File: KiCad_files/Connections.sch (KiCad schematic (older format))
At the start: 4 parts, among them U1 XC7A35T_CSG325

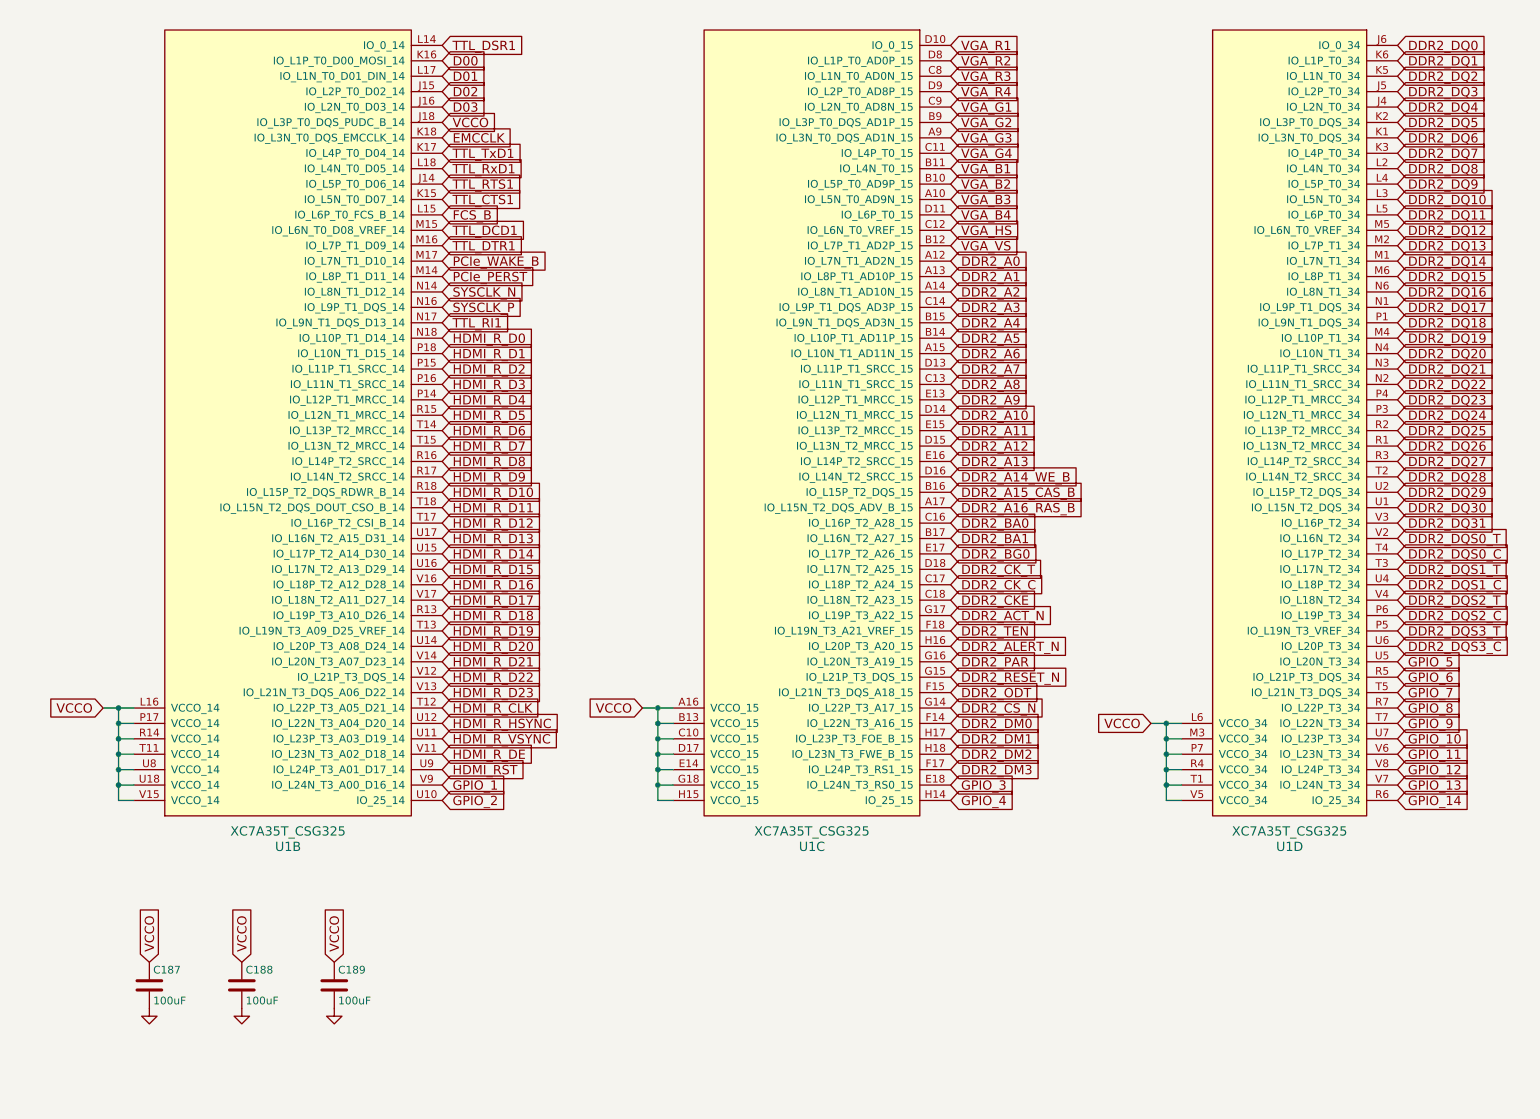
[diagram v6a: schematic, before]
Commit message: HDMI_VGA is good. Need 5V for HDMI
TODO: DDR2, connections, power
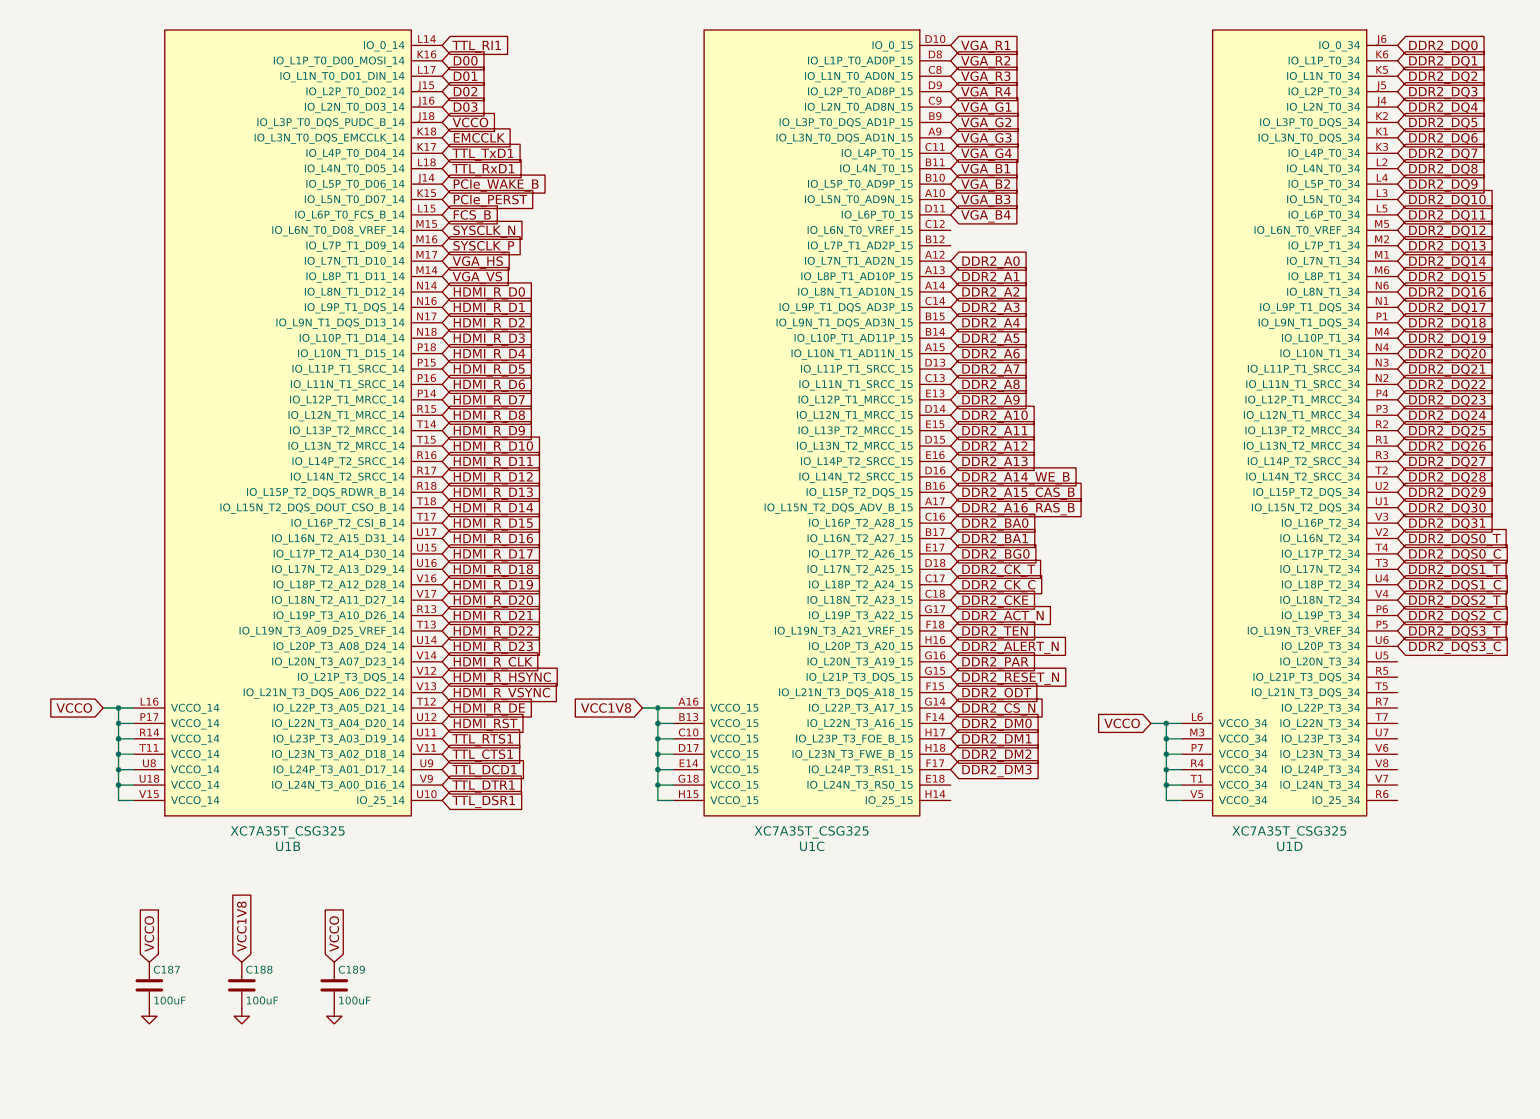
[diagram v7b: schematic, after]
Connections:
- net GPIO_1 is gone; now on net TTL_DTR1: U1.V9 (IO_L24N_T3_A00_D16_14)
- net GPIO_2 is gone; now on net TTL_DSR1: U1.U10 (IO_25_14)
- net HDMI_RST: now also U1.U12 (IO_L22N_T3_A04_D20_14); no longer U1.U9 (IO_L24P_T3_A01_D17_14)
- net HDMI_R_CLK: now also U1.V14 (IO_L20N_T3_A07_D23_14); no longer U1.T12 (IO_L22P_T3_A05_D21_14)
- net HDMI_R_D0: now also U1.N14 (IO_L8N_T1_D12_14); no longer U1.N18 (IO_L10P_T1_D14_14)
- net HDMI_R_D1: now also U1.N16 (IO_L9P_T1_DQS_14); no longer U1.P18 (IO_L10N_T1_D15_14)
- net HDMI_R_D10: now also U1.T15 (IO_L13N_T2_MRCC_14); no longer U1.R18 (IO_L15P_T2_DQS_RDWR_B_14)
- net HDMI_R_D11: now also U1.R16 (IO_L14P_T2_SRCC_14); no longer U1.T18 (IO_L15N_T2_DQS_DOUT_CSO_B_14)
- net HDMI_R_D12: now also U1.R17 (IO_L14N_T2_SRCC_14); no longer U1.T17 (IO_L16P_T2_CSI_B_14)
- net HDMI_R_D13: now also U1.R18 (IO_L15P_T2_DQS_RDWR_B_14); no longer U1.U17 (IO_L16N_T2_A15_D31_14)
- net HDMI_R_D14: now also U1.T18 (IO_L15N_T2_DQS_DOUT_CSO_B_14); no longer U1.U15 (IO_L17P_T2_A14_D30_14)
- net HDMI_R_D15: now also U1.T17 (IO_L16P_T2_CSI_B_14); no longer U1.U16 (IO_L17N_T2_A13_D29_14)
- net HDMI_R_D16: now also U1.U17 (IO_L16N_T2_A15_D31_14); no longer U1.V16 (IO_L18P_T2_A12_D28_14)
- net HDMI_R_D17: now also U1.U15 (IO_L17P_T2_A14_D30_14); no longer U1.V17 (IO_L18N_T2_A11_D27_14)
- net HDMI_R_D18: now also U1.U16 (IO_L17N_T2_A13_D29_14); no longer U1.R13 (IO_L19P_T3_A10_D26_14)
- net HDMI_R_D19: now also U1.V16 (IO_L18P_T2_A12_D28_14); no longer U1.T13 (IO_L19N_T3_A09_D25_VREF_14)
- net HDMI_R_D2: now also U1.N17 (IO_L9N_T1_DQS_D13_14); no longer U1.P15 (IO_L11P_T1_SRCC_14)
- net HDMI_R_D20: now also U1.V17 (IO_L18N_T2_A11_D27_14); no longer U1.U14 (IO_L20P_T3_A08_D24_14)
- net HDMI_R_D21: now also U1.R13 (IO_L19P_T3_A10_D26_14); no longer U1.V14 (IO_L20N_T3_A07_D23_14)
- net HDMI_R_D22: now also U1.T13 (IO_L19N_T3_A09_D25_VREF_14); no longer U1.V12 (IO_L21P_T3_DQS_14)
- net HDMI_R_D23: now also U1.U14 (IO_L20P_T3_A08_D24_14); no longer U1.V13 (IO_L21N_T3_DQS_A06_D22_14)
- net HDMI_R_D3: now also U1.N18 (IO_L10P_T1_D14_14); no longer U1.P16 (IO_L11N_T1_SRCC_14)
- net HDMI_R_D4: now also U1.P18 (IO_L10N_T1_D15_14); no longer U1.P14 (IO_L12P_T1_MRCC_14)
- net HDMI_R_D5: now also U1.P15 (IO_L11P_T1_SRCC_14); no longer U1.R15 (IO_L12N_T1_MRCC_14)
- net HDMI_R_D6: now also U1.P16 (IO_L11N_T1_SRCC_14); no longer U1.T14 (IO_L13P_T2_MRCC_14)
- net HDMI_R_D7: now also U1.P14 (IO_L12P_T1_MRCC_14); no longer U1.T15 (IO_L13N_T2_MRCC_14)
- net HDMI_R_D8: now also U1.R15 (IO_L12N_T1_MRCC_14); no longer U1.R16 (IO_L14P_T2_SRCC_14)
- net HDMI_R_D9: now also U1.T14 (IO_L13P_T2_MRCC_14); no longer U1.R17 (IO_L14N_T2_SRCC_14)
- net HDMI_R_DE: now also U1.T12 (IO_L22P_T3_A05_D21_14); no longer U1.V11 (IO_L23N_T3_A02_D18_14)
- net HDMI_R_HSYNC: now also U1.V12 (IO_L21P_T3_DQS_14); no longer U1.U12 (IO_L22N_T3_A04_D20_14)
- net HDMI_R_VSYNC: now also U1.V13 (IO_L21N_T3_DQS_A06_D22_14); no longer U1.U11 (IO_L23P_T3_A03_D19_14)
- net PCIe_PERST: now also U1.K15 (IO_L5N_T0_D07_14); no longer U1.M14 (IO_L8P_T1_D11_14)
- net PCIe_WAKE_B: now also U1.J14 (IO_L5P_T0_D06_14); no longer U1.M17 (IO_L7N_T1_D10_14)
- net SYSCLK_N: now also U1.M15 (IO_L6N_T0_D08_VREF_14); no longer U1.N14 (IO_L8N_T1_D12_14)
- net SYSCLK_P: now also U1.M16 (IO_L7P_T1_D09_14); no longer U1.N16 (IO_L9P_T1_DQS_14)
- net TTL_CTS1: now also U1.V11 (IO_L23N_T3_A02_D18_14); no longer U1.K15 (IO_L5N_T0_D07_14)
- net TTL_DCD1: now also U1.U9 (IO_L24P_T3_A01_D17_14); no longer U1.M15 (IO_L6N_T0_D08_VREF_14)
- net TTL_DSR1: no longer U1.L14 (IO_0_14)
- net TTL_DTR1: no longer U1.M16 (IO_L7P_T1_D09_14)
- net TTL_RI1: now also U1.L14 (IO_0_14); no longer U1.N17 (IO_L9N_T1_DQS_D13_14)
- net TTL_RTS1: now also U1.U11 (IO_L23P_T3_A03_D19_14); no longer U1.J14 (IO_L5P_T0_D06_14)
- net VCCO: no longer C188.1, U1.A16 (VCCO_15), U1.B13 (VCCO_15), U1.C10 (VCCO_15), U1.D17 (VCCO_15), U1.E14 (VCCO_15), U1.G18 (VCCO_15), U1.H15 (VCCO_15)
- net VGA_HS: now also U1.M17 (IO_L7N_T1_D10_14); no longer U1.C12 (IO_L6N_T0_VREF_15)
- net VGA_VS: now also U1.M14 (IO_L8P_T1_D11_14); no longer U1.B12 (IO_L7P_T1_AD2P_15)
- net GPIO_10: no longer names the net of U1.U7 (IO_L23P_T3_34)
- net GPIO_11: no longer names the net of U1.V6 (IO_L23N_T3_34)
- net GPIO_12: no longer names the net of U1.V8 (IO_L24P_T3_34)
- net GPIO_13: no longer names the net of U1.V7 (IO_L24N_T3_34)
- net GPIO_14: no longer names the net of U1.R6 (IO_25_34)
- net GPIO_3: no longer names the net of U1.E18 (IO_L24N_T3_RS0_15)
- net GPIO_4: no longer names the net of U1.H14 (IO_25_15)
- net GPIO_5: no longer names the net of U1.U5 (IO_L20N_T3_34)
- net GPIO_6: no longer names the net of U1.R5 (IO_L21P_T3_DQS_34)
- net GPIO_7: no longer names the net of U1.T5 (IO_L21N_T3_DQS_34)
- net GPIO_8: no longer names the net of U1.R7 (IO_L22P_T3_34)
- net GPIO_9: no longer names the net of U1.T7 (IO_L22N_T3_34)
- new net VCC1V8: C188.1, U1.A16 (VCCO_15), U1.B13 (VCCO_15), U1.C10 (VCCO_15), U1.D17 (VCCO_15), U1.E14 (VCCO_15), U1.G18 (VCCO_15), U1.H15 (VCCO_15)
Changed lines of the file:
@@
 $Descr A4 11693 8268
 encoding utf-8
-Sheet 6 10
+Sheet 6 9
 Title "Reconfigurable Application-Specific Accelerator Card"
 Date "2018-11-27"
@@
 	1    0    0    -1
 $EndComp
-Text GLabel 3200 2500 2    60   Input ~ 0
+Text GLabel 3200 2000 2    60   Input ~ 0
 PCIe_WAKE_B
-Text GLabel 3200 2600 2    60   Input ~ 0
+Text GLabel 3200 2100 2    60   Input ~ 0
 PCIe_PERST
 Text GLabel 3200 1600 2    60   Input ~ 0
 VCCO
 Text GLabel 4500 5400 0    60   Input ~ 0
-VCCO
+VCC1V8
 Wire Wire Line
 	4500 5400 4600 5400
@@
 $EndComp
 Text GLabel 1900 7050 1    60   Input ~ 0
-VCCO
+VCC1V8
 $Comp
 L power:GND #PWR098
@@
 	7900 5600 8000 5600
 Connection ~ 7900 5600
+Text GLabel 3200 2700 2    60   Input ~ 0
+HDMI_R_D0
+Text GLabel 3200 2800 2    60   Input ~ 0
+HDMI_R_D1
+Text GLabel 3200 2900 2    60   Input ~ 0
+HDMI_R_D2
 Text GLabel 3200 3000 2    60   Input ~ 0
-HDMI_R_D0
+HDMI_R_D3
 Text GLabel 3200 3100 2    60   Input ~ 0
-HDMI_R_D1
+HDMI_R_D4
 Text GLabel 3200 3200 2    60   Input ~ 0
-HDMI_R_D2
+HDMI_R_D5
 Text GLabel 3200 3300 2    60   Input ~ 0
-HDMI_R_D3
+HDMI_R_D6
 Text GLabel 3200 3400 2    60   Input ~ 0
-HDMI_R_D4
+HDMI_R_D7
 Text GLabel 3200 3500 2    60   Input ~ 0
-HDMI_R_D5
+HDMI_R_D8
 Text GLabel 3200 3600 2    60   Input ~ 0
-HDMI_R_D6
+HDMI_R_D9
 Text GLabel 3200 3700 2    60   Input ~ 0
-HDMI_R_D7
+HDMI_R_D10
 Text GLabel 3200 3800 2    60   Input ~ 0
-HDMI_R_D8
+HDMI_R_D11
 Text GLabel 3200 3900 2    60   Input ~ 0
-HDMI_R_D9
+HDMI_R_D12
 Text GLabel 3200 4000 2    60   Input ~ 0
-HDMI_R_D10
+HDMI_R_D13
 Text GLabel 3200 4100 2    60   Input ~ 0
-HDMI_R_D11
+HDMI_R_D14
 Text GLabel 3200 4200 2    60   Input ~ 0
-HDMI_R_D12
+HDMI_R_D15
 Text GLabel 3200 4300 2    60   Input ~ 0
-HDMI_R_D13
+HDMI_R_D16
 Text GLabel 3200 4400 2    60   Input ~ 0
-HDMI_R_D14
+HDMI_R_D17
 Text GLabel 3200 4500 2    60   Input ~ 0
-HDMI_R_D15
+HDMI_R_D18
 Text GLabel 3200 4600 2    60   Input ~ 0
-HDMI_R_D16
+HDMI_R_D19
 Text GLabel 3200 4700 2    60   Input ~ 0
-HDMI_R_D17
+HDMI_R_D20
 Text GLabel 3200 4800 2    60   Input ~ 0
-HDMI_R_D18
+HDMI_R_D21
 Text GLabel 3200 4900 2    60   Input ~ 0
-HDMI_R_D19
+HDMI_R_D22
 Text GLabel 3200 5000 2    60   Input ~ 0
-HDMI_R_D20
+HDMI_R_D23
 Text GLabel 3200 5100 2    60   Input ~ 0
-HDMI_R_D21
+HDMI_R_CLK
+Text GLabel 3200 5500 2    60   Input ~ 0
+HDMI_RST
 Text GLabel 3200 5200 2    60   Input ~ 0
-HDMI_R_D22
+HDMI_R_HSYNC
 Text GLabel 3200 5300 2    60   Input ~ 0
-HDMI_R_D23
+HDMI_R_VSYNC
 Text GLabel 3200 5400 2    60   Input ~ 0
-HDMI_R_CLK
-Text GLabel 3200 5800 2    60   Input ~ 0
-HDMI_RST
-Text GLabel 3200 5500 2    60   Input ~ 0
-HDMI_R_HSYNC
-Text GLabel 3200 5600 2    60   Input ~ 0
-HDMI_R_VSYNC
-Text GLabel 3200 5700 2    60   Input ~ 0
 HDMI_R_DE
 Text GLabel 3200 1800 2    60   Input ~ 0
@@
 Text GLabel 3200 1900 2    60   Input ~ 0
 TTL_RxD1
-Text GLabel 3200 2000 2    60   Input ~ 0
+Text GLabel 3200 5600 2    60   Input ~ 0
 TTL_RTS1
-Text GLabel 3200 2100 2    60   Input ~ 0
+Text GLabel 3200 5700 2    60   Input ~ 0
 TTL_CTS1
-Text GLabel 3200 2400 2    60   Input ~ 0
+Text GLabel 3200 5900 2    60   Input ~ 0
 TTL_DTR1
+Text GLabel 3200 6000 2    60   Input ~ 0
+TTL_DSR1
+Text GLabel 3200 5800 2    60   Input ~ 0
+TTL_DCD1
 Text GLabel 3200 1100 2    60   Input ~ 0
-TTL_DSR1
-Text GLabel 3200 2300 2    60   Input ~ 0
-TTL_DCD1
-Text GLabel 3200 2900 2    60   Input ~ 0
 TTL_RI1
 $Comp
@@
 	1    0    0    -1
 $EndComp
-Text GLabel 3200 2700 2    60   Input ~ 0
+Text GLabel 3200 2300 2    60   Input ~ 0
 SYSCLK_N
-Text GLabel 3200 2800 2    60   Input ~ 0
+Text GLabel 3200 2400 2    60   Input ~ 0
 SYSCLK_P
 Text GLabel 6500 1100 2    60   Input ~ 0
@@
 Text GLabel 6500 2200 2    60   Input ~ 0
 VGA_B4
-Text GLabel 6500 2300 2    60   Input ~ 0
+Text GLabel 3200 2500 2    60   Input ~ 0
 VGA_HS
-Text GLabel 6500 2400 2    60   Input ~ 0
+Text GLabel 3200 2600 2    60   Input ~ 0
 VGA_VS
 Text GLabel 6500 2500 2    60   Input ~ 0
@@
 Text GLabel 6500 5800 2    60   Input ~ 0
 DDR2_DM3
-Text GLabel 3200 5900 2    60   Input ~ 0
-GPIO_1
-Text GLabel 3200 6000 2    60   Input ~ 0
-GPIO_2
-Text GLabel 6500 5900 2    60   Input ~ 0
-GPIO_3
-Text GLabel 6500 6000 2    60   Input ~ 0
-GPIO_4
-Text GLabel 9400 5100 2    60   Input ~ 0
-GPIO_5
-Text GLabel 9400 5200 2    60   Input ~ 0
-GPIO_6
-Text GLabel 9400 5300 2    60   Input ~ 0
-GPIO_7
-Text GLabel 9400 5400 2    60   Input ~ 0
-GPIO_8
-Text GLabel 9400 5500 2    60   Input ~ 0
-GPIO_9
-Text GLabel 9400 5600 2    60   Input ~ 0
-GPIO_10
-Text GLabel 9400 5700 2    60   Input ~ 0
-GPIO_11
-Text GLabel 9400 5800 2    60   Input ~ 0
-GPIO_12
-Text GLabel 9400 5900 2    60   Input ~ 0
-GPIO_13
-Text GLabel 9400 6000 2    60   Input ~ 0
-GPIO_14
 Wire Wire Line
 	1100 5400 1200 5400
